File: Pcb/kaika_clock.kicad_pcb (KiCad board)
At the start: 2 copper layers, 128 x 32 mm, 30 parts, among them J1 Conn_01x04, J6 Conn_01x04, SW1 Reset, U1 AMS1117-3.3, U2 STM32F103C8Tx, U3 DS3231MZ, U4 TYPE-C-31-M-12, Y1 Crystal

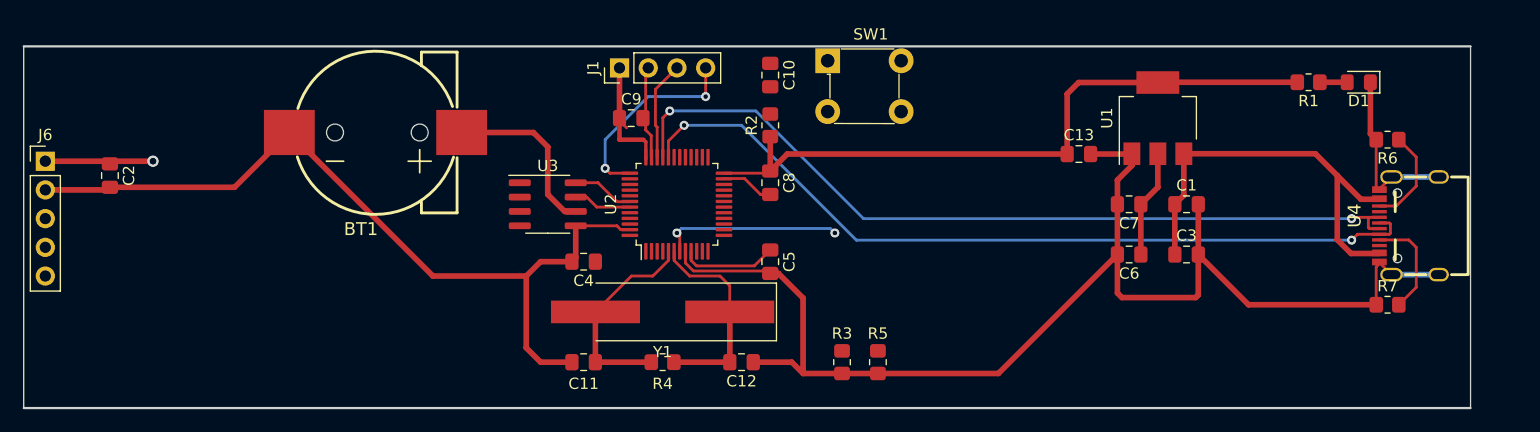
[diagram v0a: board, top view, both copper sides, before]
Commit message: change usb to micro usb
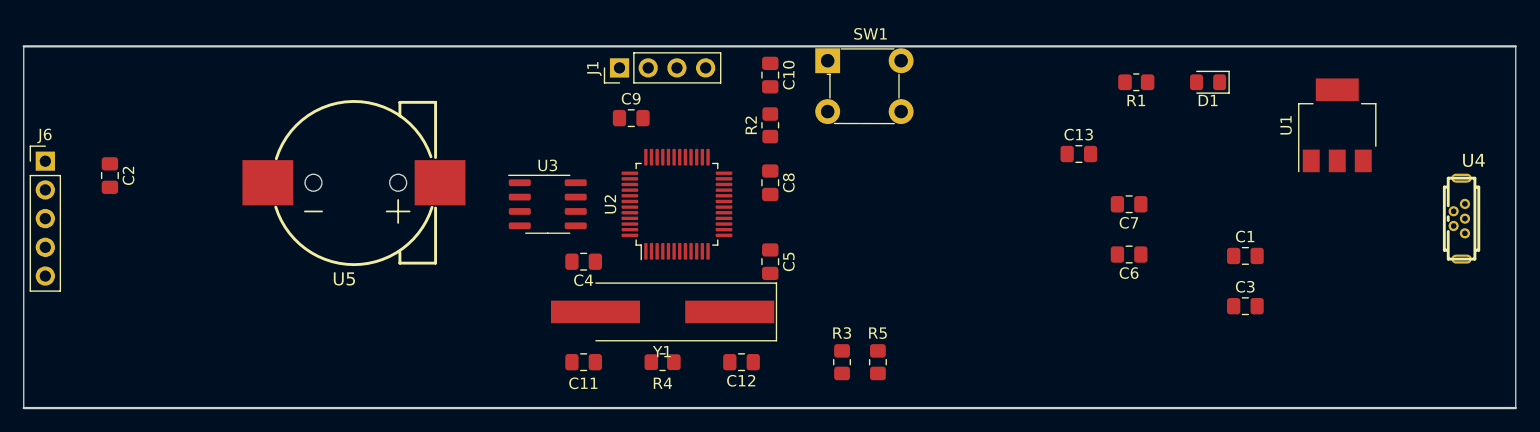
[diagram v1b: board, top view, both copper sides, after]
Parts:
- removed BT1: Battery_Cell, Kaka:BAT-SMD_CR1220-2
- removed R6, R7: 10K, Resistor_SMD:R_0805_2012Metric_Pad1.20x1.40mm_HandSolder
- added U5: CR1220-2, Kaka-footprints:BAT-SMD_CR1220-2, F.Cu at (69.2, 52.7)
- U4: value TYPE-C-31-M-12 -> MICRO-USB_TH; footprint Kaka:USB-C_SMD-TYPE-C-31-M-12 -> Kaka-footprints:MICRO-USB-TH_MICRO-USB-A14
- moved U1 15.9 mm to (156.2, 47.6)
- moved R1 15.2 mm to (138.4, 43.8)
- moved D1 13.3 mm to (144.8, 43.8)
- moved C1 6.93 mm to (148.1, 59.2)
- moved C3 6.93 mm to (148.1, 63.6)
- moved U4 4.49 mm to (167.0, 55.9), turned to 0 degrees
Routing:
- net GND: track 218.1 -> 0.00 mm
- net +3V3: track 99.4 -> 0.00 mm, vias 1 -> 0
- net USB_DP: track 73.1 -> 0.00 mm, vias 2 -> 0
- net USB_DM: track 72.2 -> 0.00 mm, vias 2 -> 0
- net VCC: track 38.1 -> 0.00 mm
- net OSC_IN: track 19.6 -> 0.00 mm
- net OSC_OUT: track 18.4 -> 0.00 mm
- net SWCLK: track 17.9 -> 0.00 mm, vias 2 -> 0
- net RESET: track 16.0 -> 0.00 mm, vias 2 -> 0
- net Net-(U3-Pad6): track 15.5 -> 0.00 mm
- net Net-(R7-Pad2): track 9.25 -> 0.00 mm
- net SWDIO: track 8.76 -> 0.00 mm
- net Net-(R6-Pad1): track 8.73 -> 0.00 mm
- net I2C1_SCL: track 5.50 -> 0.00 mm
- net I2C1_SDA: track 5.16 -> 0.00 mm
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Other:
- board size 128 x 32 mm -> 132 x 32 mm

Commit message: modify the pcb
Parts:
- added REF**: MountingHole_2.2mm_M2, MountingHole:MountingHole_2.2mm_M2, F.Cu at (169.5, 43.8)
- added REF**: MountingHole_2.2mm_M2, MountingHole:MountingHole_2.2mm_M2, F.Cu at (168.9, 69.8)
- added REF**: MountingHole_2.2mm_M2, MountingHole:MountingHole_2.2mm_M2, F.Cu at (42.5, 70.5)
- added REF**: MountingHole_2.2mm_M2, MountingHole:MountingHole_2.2mm_M2, F.Cu at (43.2, 43.8)
- moved U5 63.1 mm to (132.1, 58.4), turned to 270 degrees
- moved U3 29.2 mm to (115.6, 55.9), turned to 180 degrees
- moved R2 28.2 mm to (134.0, 43.8)
- moved SW1 27.9 mm to (139.1, 42.5)
- moved R1 26.3 mm to (164.5, 47.6)
- moved D1 25.1 mm to (169.5, 47.6)
- moved U1 20.1 mm to (149.9, 66.7), turned to 180 degrees
- moved C1 18.9 mm to (165.1, 67.3), turned to 270 degrees
- moved C7 18.0 mm to (155.6, 57.1)
- moved C13 17.8 mm to (151.1, 51.0), turned to 270 degrees
- moved C6 17.8 mm to (155.6, 59.7)
- moved U4 13.1 mm to (160.7, 67.3)
- moved C3 7.62 mm to (155.6, 62.2), turned to 180 degrees
- moved C4 2.01 mm to (90.2, 57.8), turned to 90 degrees
- moved Y1 1.27 mm to (96.5, 62.9)
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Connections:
- U4 pad 7: (no net) -> GND
